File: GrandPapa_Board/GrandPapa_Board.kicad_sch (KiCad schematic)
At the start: 12 parts, among them J1 Conn_01x03_Female, J11 Conn_01x04_Male, J2 Conn_02x06, J3 M80-5000642, J4 M80-5000642, J5 M80-5000642

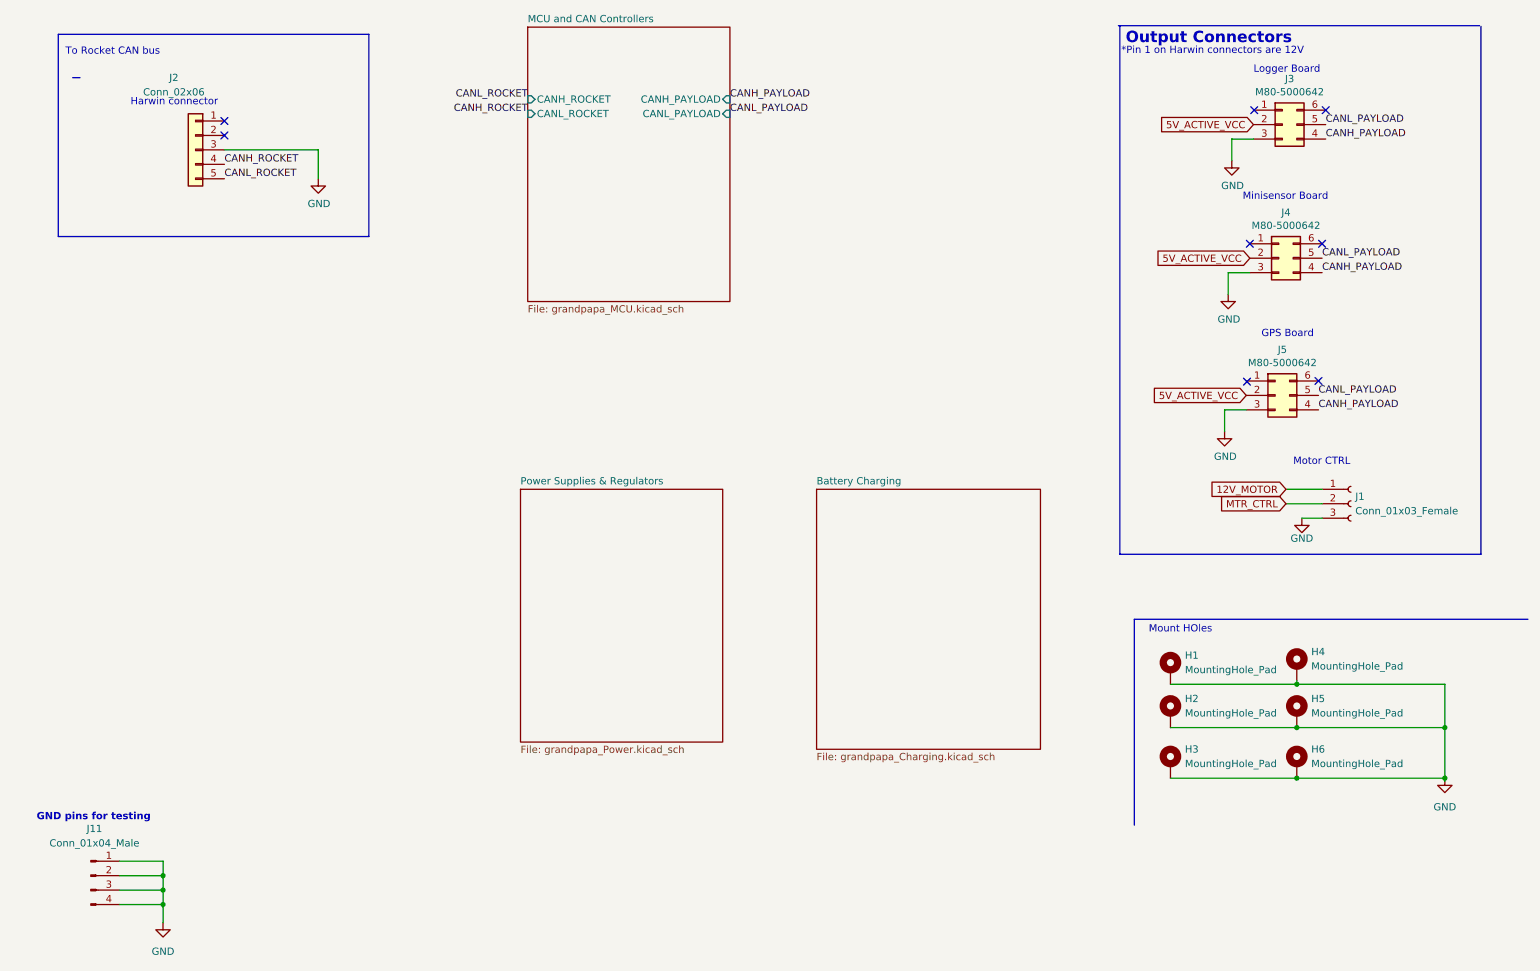
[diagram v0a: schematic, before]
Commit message: Remove 3.3V, placeholders for battery charge IC and 5V boost converter
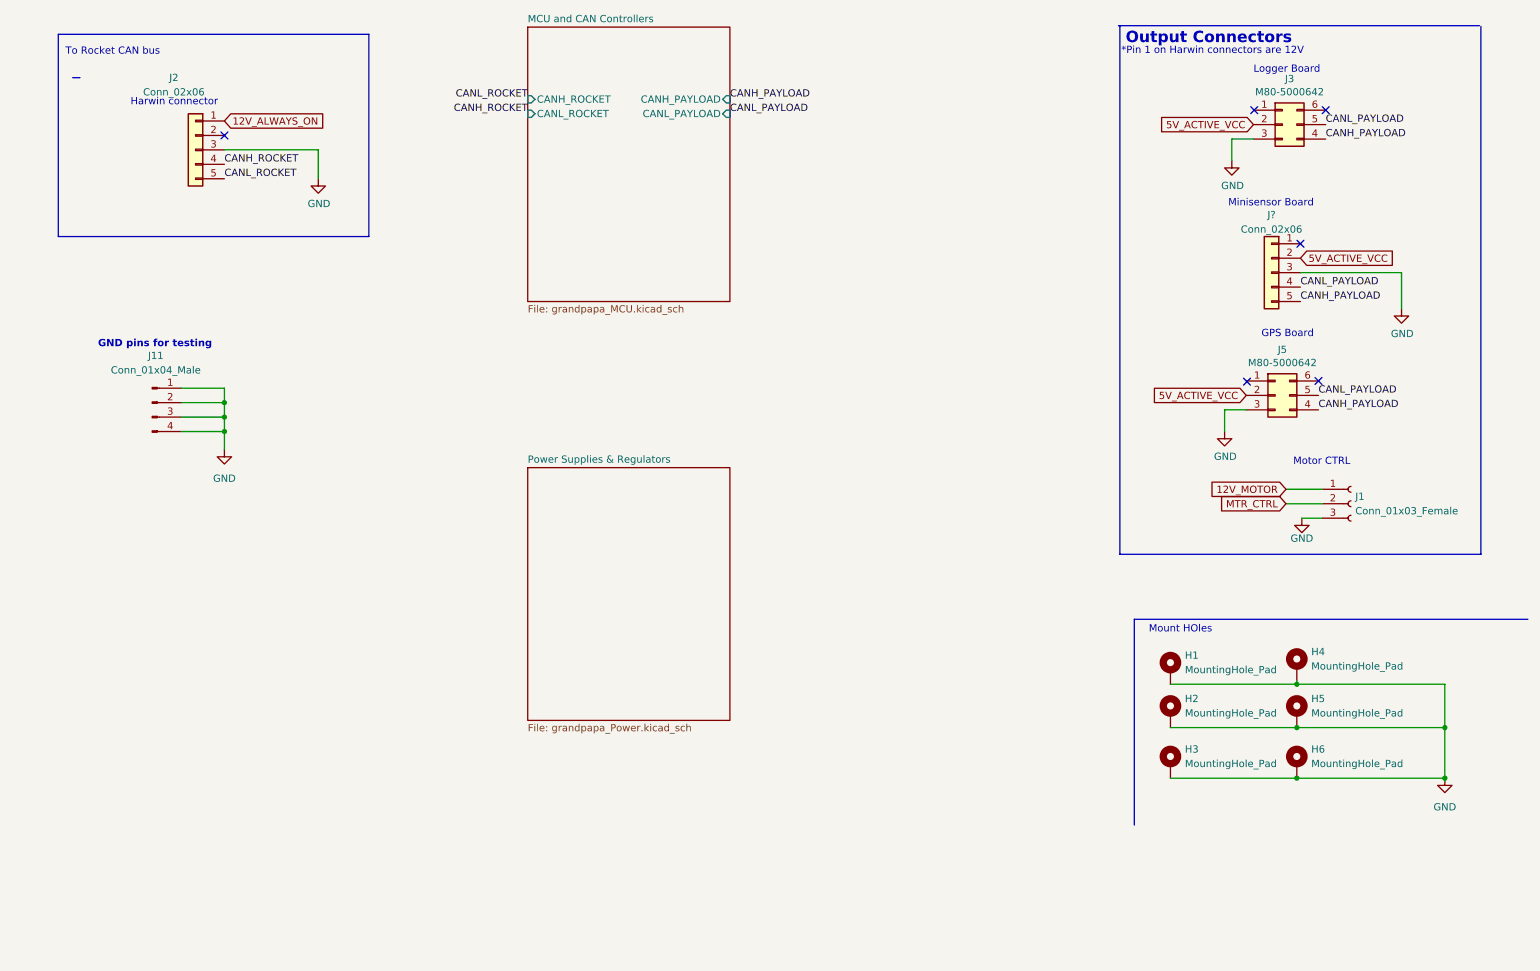
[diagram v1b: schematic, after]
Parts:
- removed J4: M80-5000642, Payload2020_custom:connector_Harwin_M80-5000642, symbol Connector_Generic:Conn_02x03_Counter_Clockwise
- added J?: Conn_02x06, Payload2020_custom:connector_Harwin_M80-5000642, symbol Connector_Generic:Conn_01x05
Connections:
- net 5V_ACTIVE_VCC: now also J?.2 (Pin_2)
- net CANH_PAYLOAD: now also J?.5 (Pin_5)
- net CANL_PAYLOAD: now also J?.4 (Pin_4)
- net GND: now also J?.3 (Pin_3)
- net 12V_ALWAYS_ON: now reaches J2.1 (Pin_1)
- no-connect marks 8 -> 6
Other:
- removed sheet Battery Charging
- moved on the sheet: J11

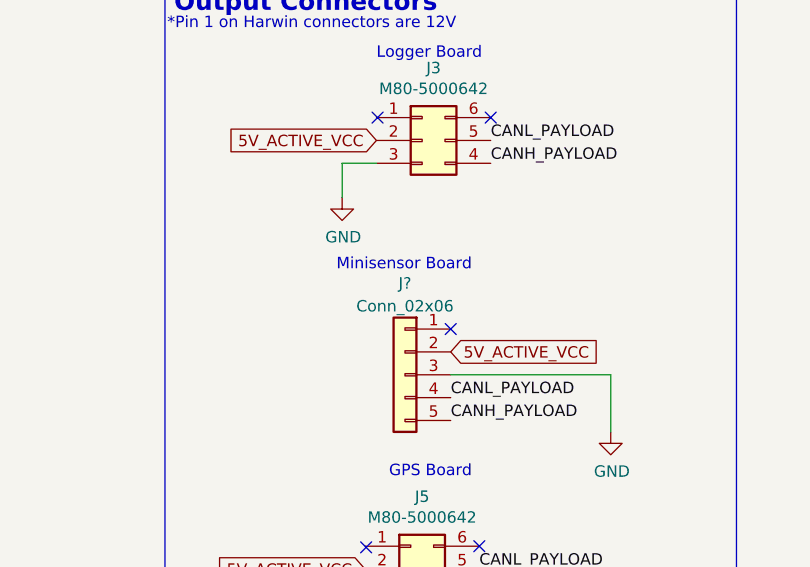
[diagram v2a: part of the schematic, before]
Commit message: add 5V boost converter and 12V load switch, finish battery charge circuit
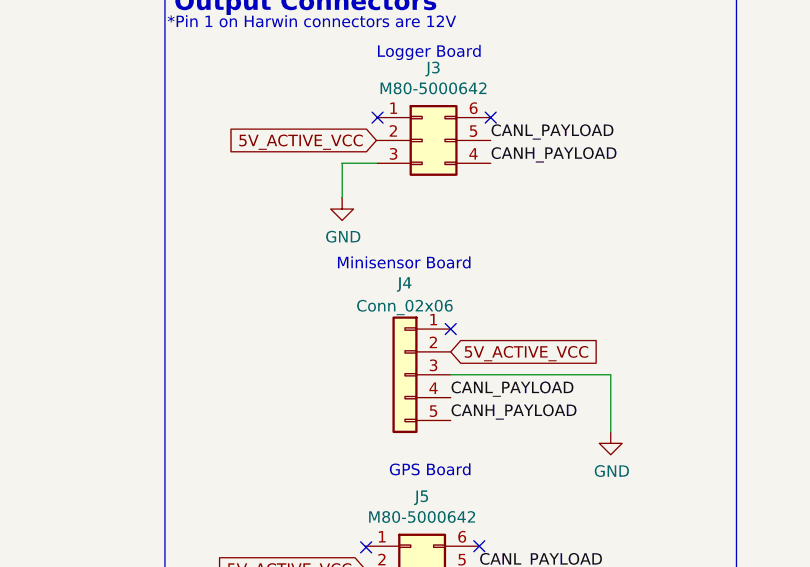
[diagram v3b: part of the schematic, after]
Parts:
- gave numbers to parts that had none: 1

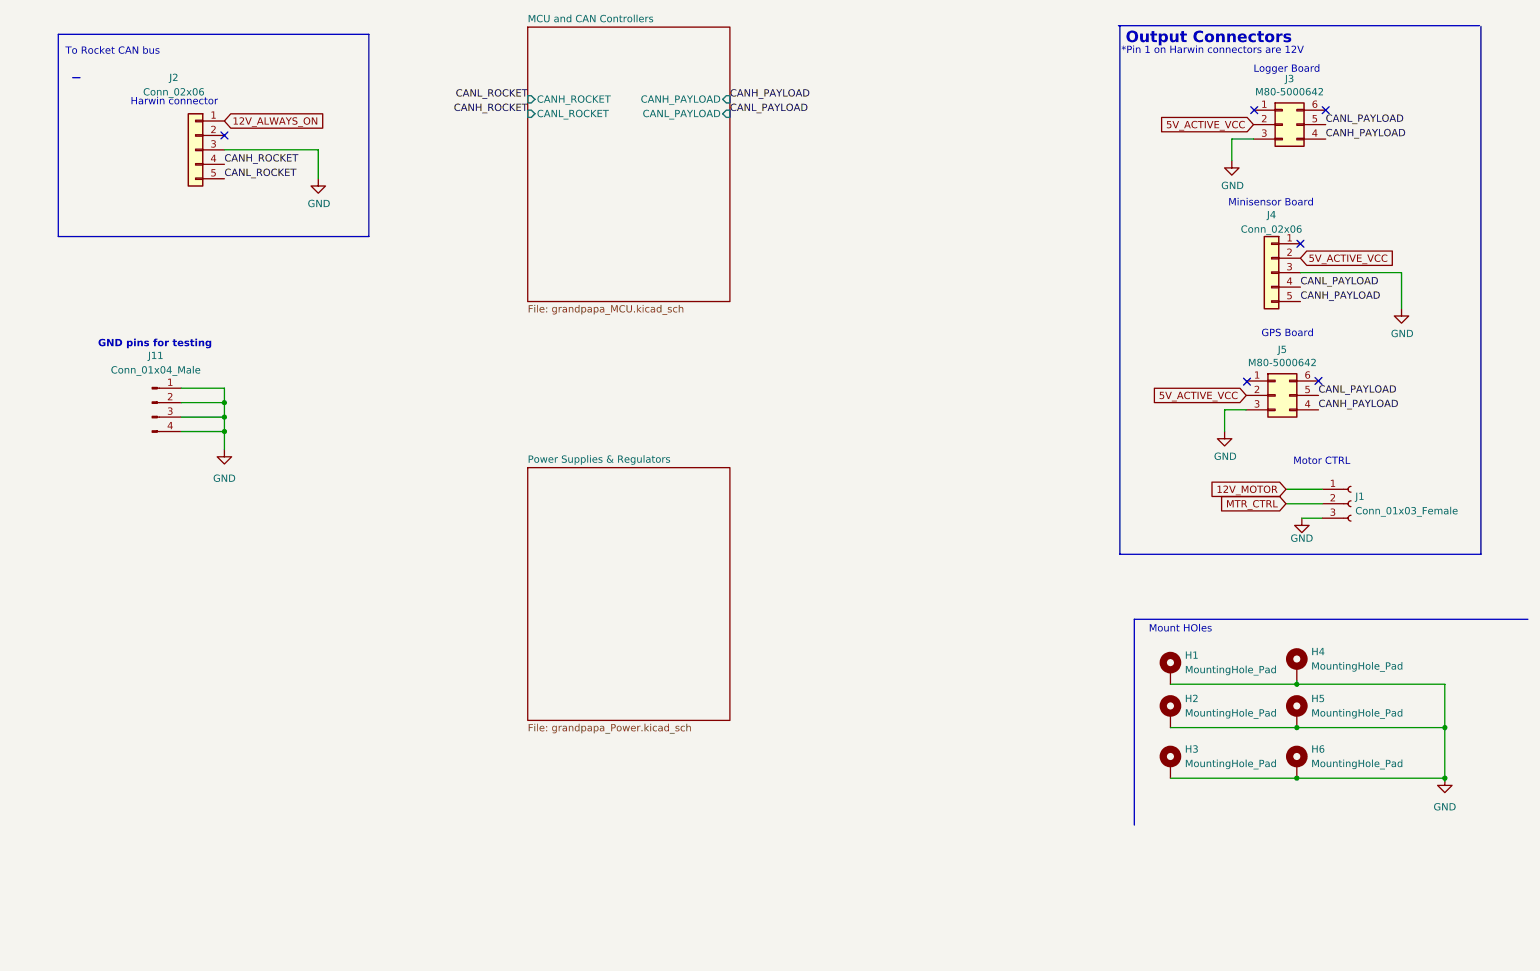
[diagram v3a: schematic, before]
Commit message: clean up schematic, fix some ERC errors
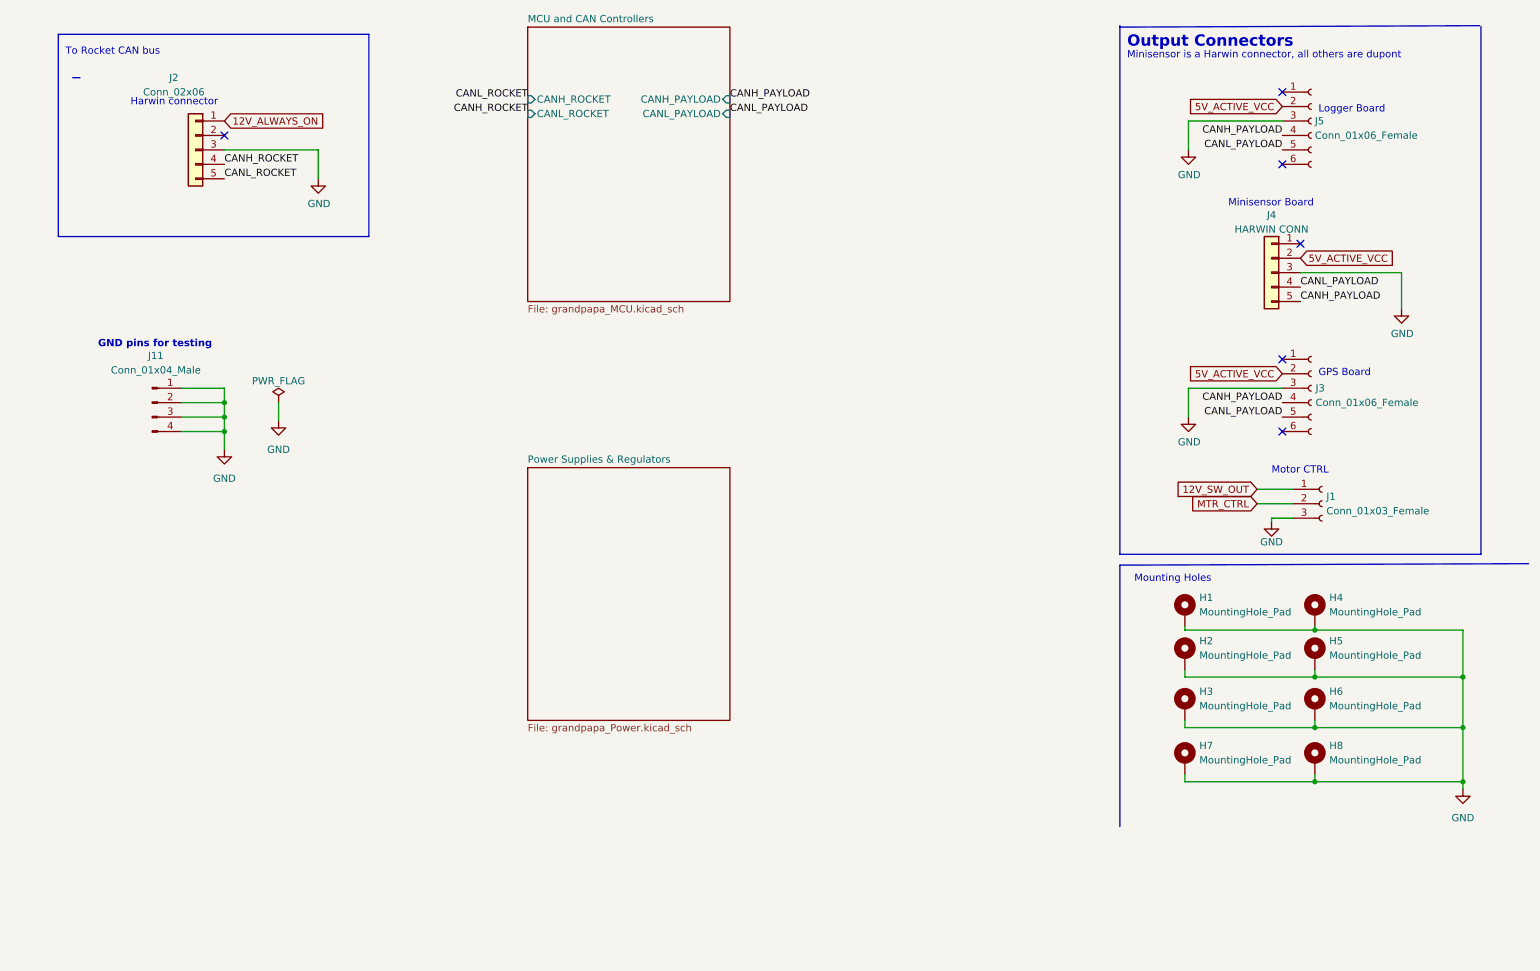
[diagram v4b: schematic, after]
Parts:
- removed J3, J5: M80-5000642, Payload2020_custom:connector_Harwin_M80-5000642, symbol Connector_Generic:Conn_02x03_Counter_Clockwise
- added H7, H8: MountingHole_Pad, symbol Mechanical:MountingHole_Pad
- added J3, J5: Conn_01x06_Female, symbol Connector:Conn_01x06_Female
- J4: value Conn_02x06 -> HARWIN CONN
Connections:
- net 5V_ACTIVE_VCC: now also J3.2 (Pin_2), J5.2 (Pin_2)
- net CANH_PAYLOAD: now also J3.4 (Pin_4), J5.4 (Pin_4)
- net CANL_PAYLOAD: now also J3.5 (Pin_5), J5.5 (Pin_5)
- net GND: now also H7.1, H8.1, J3.3 (Pin_3), J5.3 (Pin_3)
- net 12V_MOTOR renamed 12V_SW_OUT
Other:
- note added: "Minisensor is a Harwin connector, all others are dupont"
- note added: "Mounting Holes"
- note removed: "*Pin 1 on Harwin connectors are 12V"
- note removed: "Mount HOles"
- moved on the sheet: H1, H2, H3, H4, H5, H6, J1

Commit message: move 12V shutoff to reg, rm motor stuff, subsheet/global pin redesign
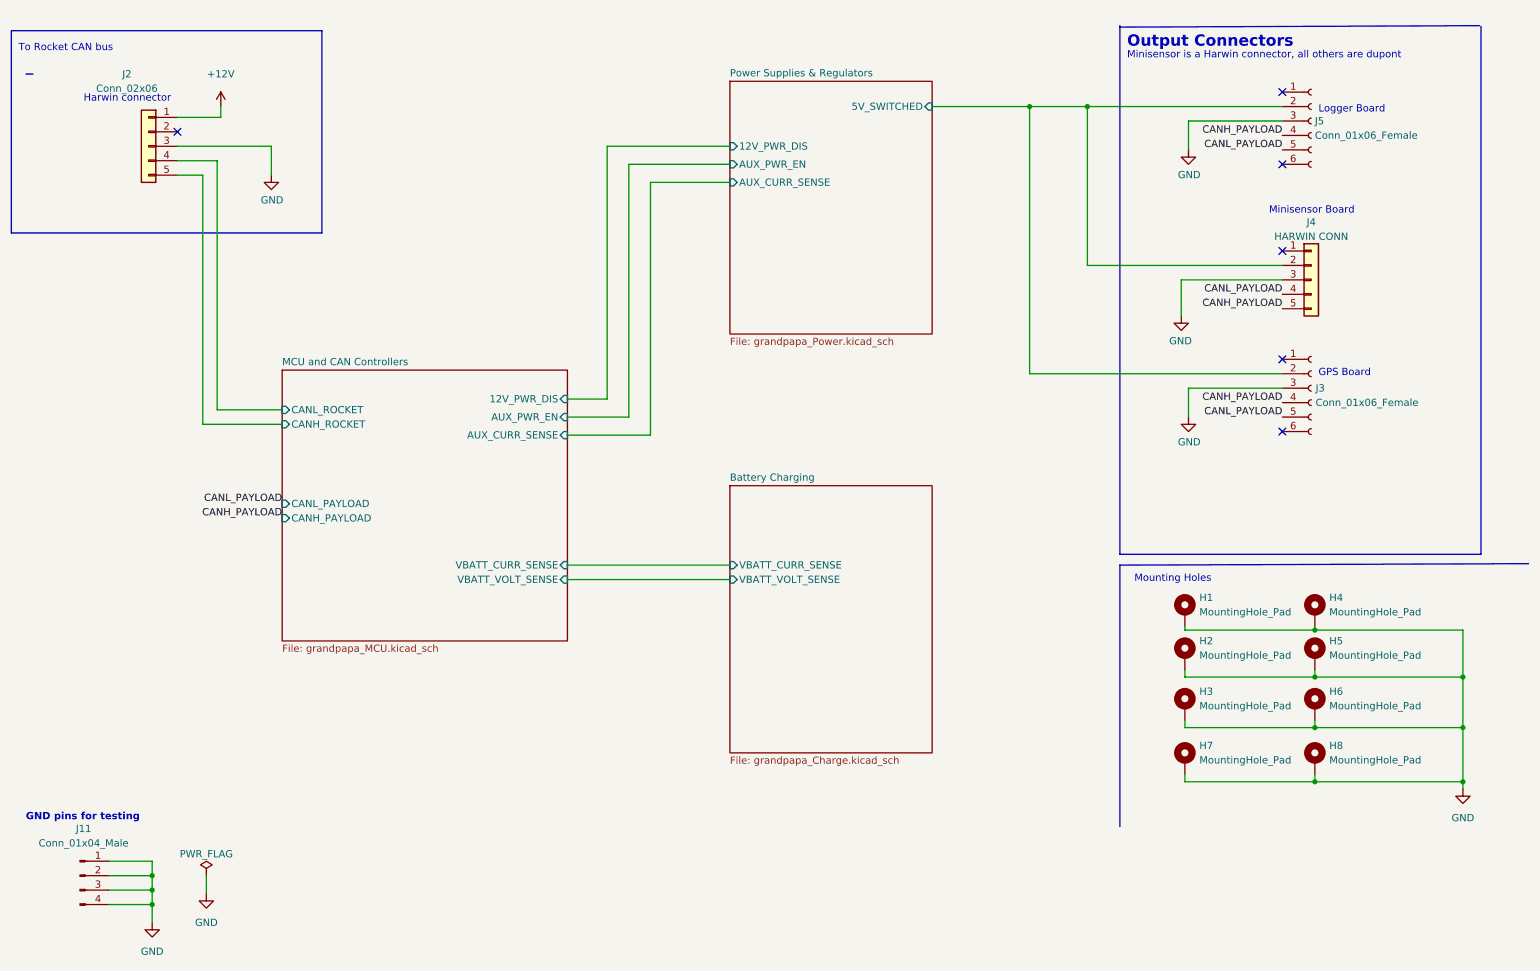
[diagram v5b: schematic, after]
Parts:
- removed J1: Conn_01x03_Female, symbol Connector:Conn_01x03_Female
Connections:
- net 12V_ALWAYS_ON renamed +12V
- net 5V_ACTIVE_VCC renamed Power Supplies & Regulators/5V_SWITCHED
- net CANH_ROCKET renamed MCU and CAN Controllers/CANL_ROCKET
- net CANL_ROCKET renamed MCU and CAN Controllers/CANH_ROCKET
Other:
- added sheet Battery Charging (grandpapa_Charge.kicad_sch)
- sheet MCU and CAN Controllers ports: added 12V_PWR_DIS, AUX_CURR_SENSE, AUX_PWR_EN, VBATT_CURR_SENSE, VBATT_VOLT_SENSE; removed none
- sheet Power Supplies & Regulators ports: added 12V_PWR_DIS, 5V_SWITCHED, AUX_CURR_SENSE, AUX_PWR_EN; removed none
- note removed: "Motor CTRL"
- moved on the sheet: J11, J2, J4
